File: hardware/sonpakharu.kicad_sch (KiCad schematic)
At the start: 66 parts, among them IC1 ESP32-S3-WROOM-1U-N4, J1 ADC4, J10 EXT2, J11 EXT3, J12 BATT, J13 EXT7, J14 PWR, J15 EXT8, J16 485, J17 FTDI, J2 ADC3, J3 ADC2, J4 ADC1, J5 EXT4, J6 I2C, J7 EXT5, J8 EXT1, J9 EXT6, Q1 DMG3415U, Q2 S8050, Q3 S8050, Q4 S8050, SW1 Boot, SW2 Reset, U1 AP2112K-3.3TRG1, U2 MCP73831-2-OT, U3 MAX485E, U4 ADS1115IDGSR

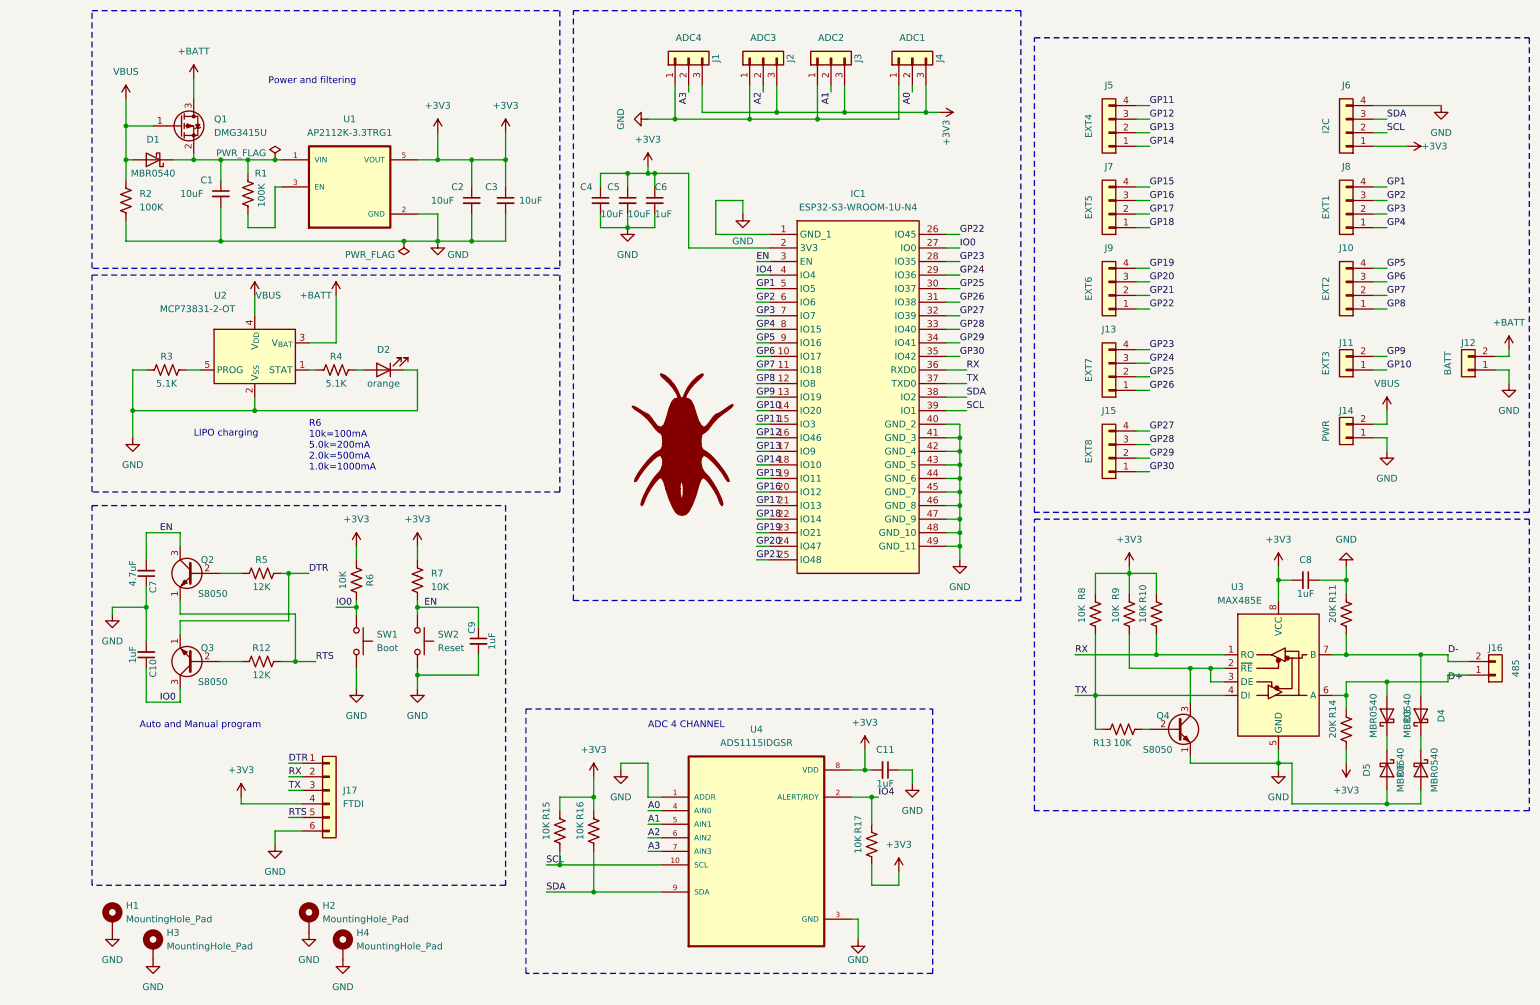
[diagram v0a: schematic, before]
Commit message: Fix: foot prints, re routed pcb, added 3d model
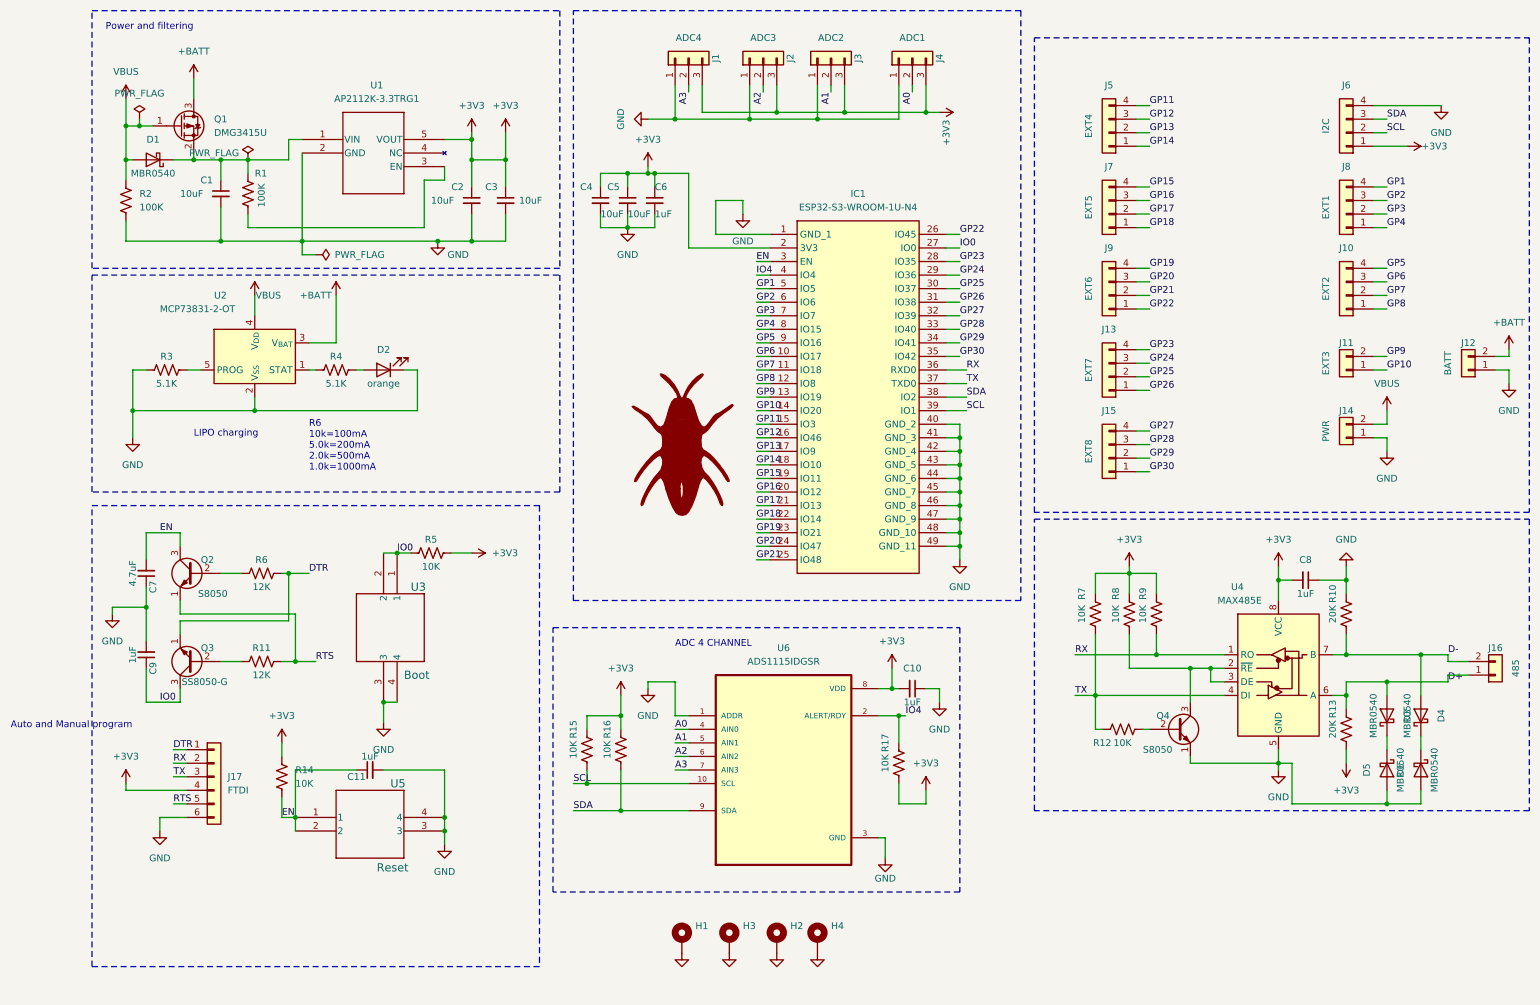
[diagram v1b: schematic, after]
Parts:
- removed SW1: Boot, Button_Switch_SMD:SW_Push_1P1T_NO_6x6mm_H9.5mm, symbol Switch:SW_Push
- removed SW2: Reset, Button_Switch_SMD:SW_Push_1P1T_NO_6x6mm_H9.5mm, symbol Switch:SW_Push
- added U3: Boot, PTS526 SK15 SMTR2 LFS:SMT_FS, symbol PTS526 SK15 SMTR2 LFS:PTS526_SK15_SMTR2_LFS
- added U5: Reset, PTS526 SK15 SMTR2 LFS:SMT_FS, symbol PTS526 SK15 SMTR2 LFS:PTS526_SK15_SMTR2_LFS
- H2: value MountingHole_Pad -> mounting hole
- Q3: value S8050 -> SS8050-G
- U1: footprint AP2112K-3.3TRG1:SOT95P285X140-5N -> AP2112K_3_3TRG1:SOT25; symbol AP2112K-3.3TRG1:AP2112K-3.3TRG1 -> AP2112K_3_3TRG1:AP2112K-3.3TRG1
- U4: renamed from U3; footprint Package_SO:SOP-8_3.9x4.9mm_P1.27mm -> Package_SO:SOIC-8_3.9x4.9mm_P1.27mm
- U6: renamed from U4; footprint ADS1115IDGSR:SOP50P490X110-10N -> Package_SO:VSSOP-10_3x3mm_P0.5mm
- renumbered C11 to C10, C9 to C11, C10 to C9, R11 to R10, R12 to R11, R13 to R12, R14 to R13, R7 to R14, R6 to R5, R5 to R6, R8 to R7, R9 to R8, R10 to R9
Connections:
- net +3V3: now also R5.2; no longer R5.1
- net EN: now also U5.1, U5.2
- net GND: now also U3.3, U3.4, U5.3, U5.4
- net IO0: now also R5.1, U3.1, U3.2; no longer R5.2
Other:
- moved on the sheet: C10, C11, H1, H2, H3, H4, J17, R14, R15, R16, R17, R5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

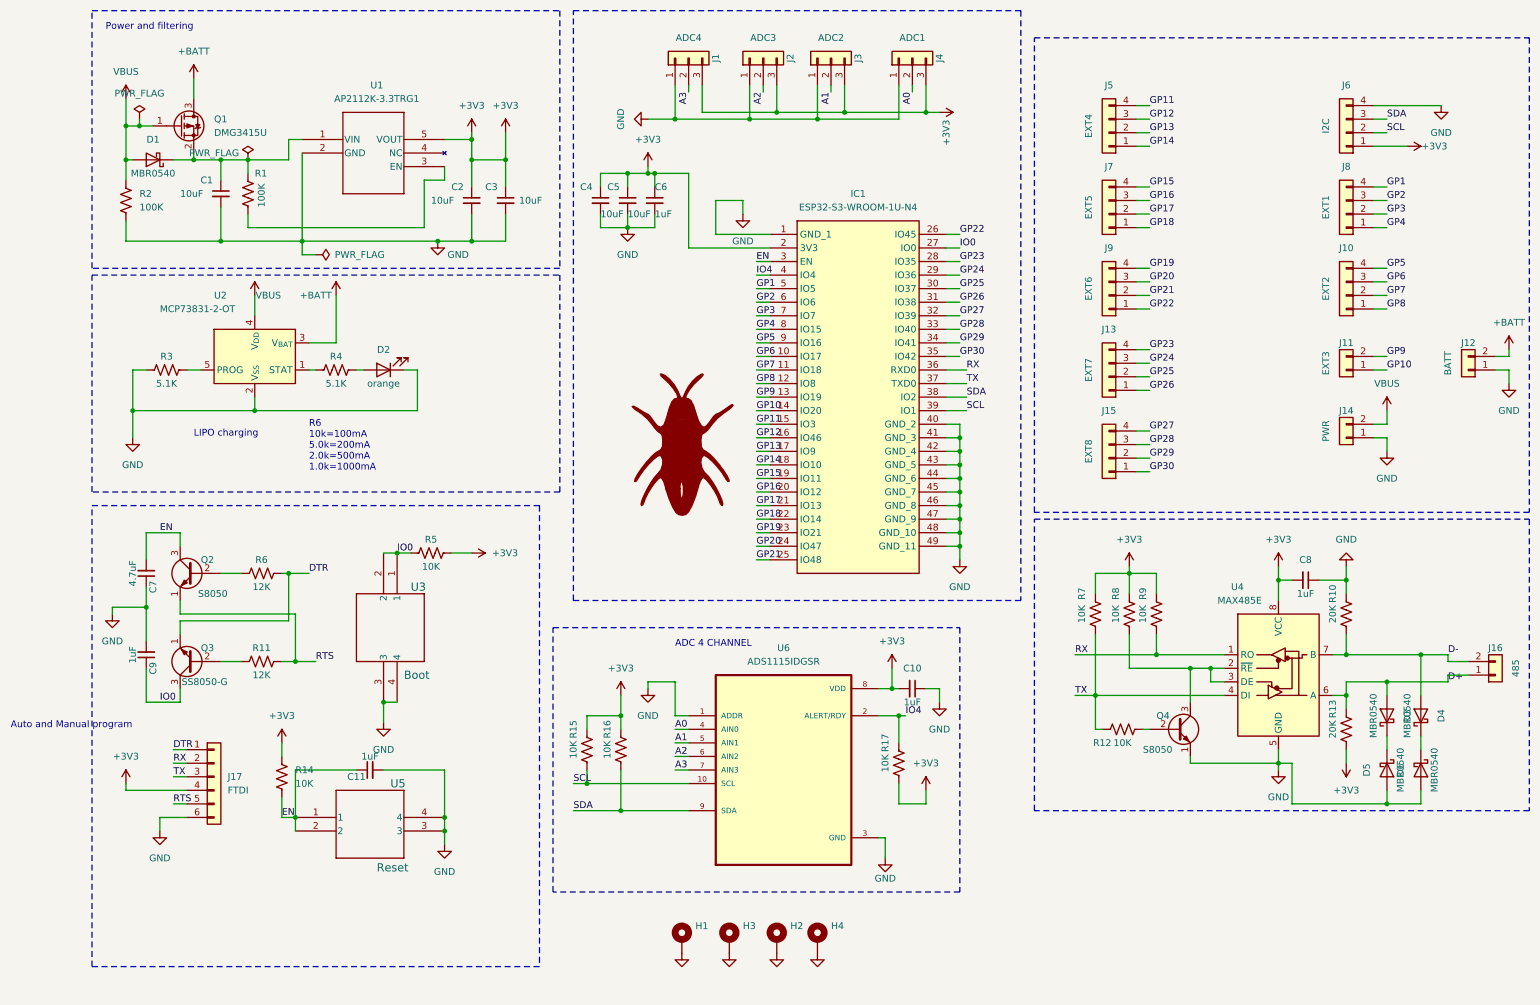
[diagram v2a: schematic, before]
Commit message: rectified sch
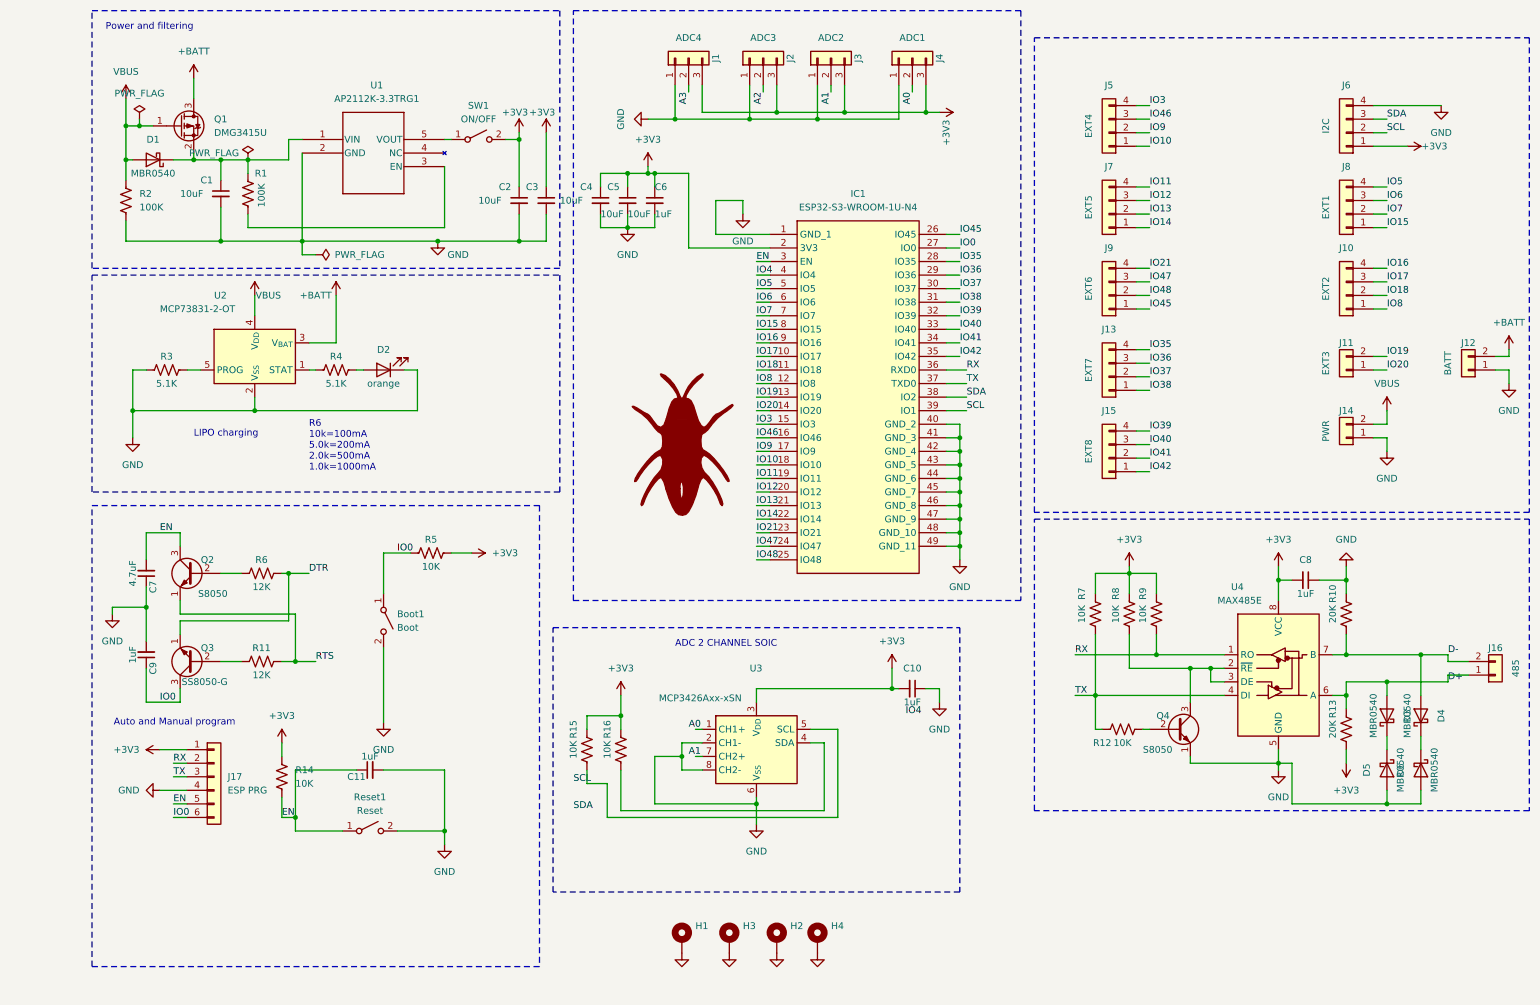
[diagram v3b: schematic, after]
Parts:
- removed R17: 10K, Resistor_SMD:R_0603_1608Metric, symbol Device:R_US
- removed U3: Boot, PTS526 SK15 SMTR2 LFS:SMT_FS, symbol PTS526 SK15 SMTR2 LFS:PTS526_SK15_SMTR2_LFS
- removed U5: Reset, PTS526 SK15 SMTR2 LFS:SMT_FS, symbol PTS526 SK15 SMTR2 LFS:PTS526_SK15_SMTR2_LFS
- removed U6: ADS1115IDGSR, Package_SO:VSSOP-10_3x3mm_P0.5mm, symbol ADS1115IDGSR:ADS1115IDGSR
- added Boot1: Boot, tactile_5.4:tactile_5.4, symbol Switch:SW_SPST
- added Reset1: Reset, tactile_5.4:tactile_5.4, symbol Switch:SW_SPST
- added SW1: ON/OFF, Connector_PinHeader_2.54mm:PinHeader_1x02_P2.54mm_Vertical, symbol Switch:SW_SPST
- added U3: MCP3426Axx-xSN, Package_SO:SOIC-8_3.9x4.9mm_P1.27mm, symbol Analog_ADC:MCP3426Axx-xSN
- C1, C10, C11, C2, C3, C4, C6, C7, C8, C9: footprint Capacitor_SMD:C_0603_1608Metric -> Capacitor_SMD:C_0805_2012Metric
- D2: footprint LED_SMD:LED_0603_1608Metric -> LED_SMD:LED_1206_3216Metric
- J17: value FTDI -> ESP PRG
- R1, R10, R11, R12, R13, R14, R15, R2, R3, R4, R5, R6, R7, R8, R9: footprint Resistor_SMD:R_0603_1608Metric -> Resistor_SMD:R_0805_2012Metric
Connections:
- net +3V3: now also J17.1 (Pin_1), SW1.2 (B), U3.3 (V_{DD}); no longer J17.4 (Pin_4), U1.5 (VOUT)
- net DTR: no longer J17.1 (Pin_1)
- net EN: now also J17.5 (Pin_5), Reset1.1 (A)
- net GND: now also J17.4 (Pin_4), Boot1.2 (B), Reset1.2 (B), U3.2 (CH1-), U3.6 (V_{SS}), U3.8 (CH2-); no longer J17.6 (Pin_6)
- net IO0: now also J17.6 (Pin_6), Boot1.1 (A)
- net RTS: no longer J17.5 (Pin_5)
- net SCL: no longer R15.2
- net SDA: no longer R16.2
- net GP1 renamed IO5
- net GP10 renamed IO20
- net GP11 renamed IO3
- net GP12 renamed IO46
- net GP13 renamed IO9
- net GP14 renamed IO10
- net GP15 renamed IO11
- net GP16 renamed IO12
- net GP17 renamed IO13
- net GP18 renamed IO14
- net GP19 renamed IO21
- net GP2 renamed IO6
- net GP20 renamed IO47
- net GP21 renamed IO48
- net GP22 renamed IO45
- net GP23 renamed IO35
- net GP24 renamed IO36
- net GP25 renamed IO37
- net GP26 renamed IO38
- net GP27 renamed IO39
- net GP28 renamed IO40
- net GP29 renamed IO41
- net GP3 renamed IO7
- net GP30 renamed IO42
- net GP4 renamed IO15
- net GP5 renamed IO16
- net GP6 renamed IO17
- net GP7 renamed IO18
- net GP8 renamed IO8
- net GP9 renamed IO19
- new net: R15.2, U3.5 (SCL)
- new net: SW1.1 (A), U1.5 (VOUT)
- new net: R16.2, U3.4 (SDA)
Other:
- note added: "ADC 2 CHANNEL SOIC"
- note removed: "ADC 4 CHANNEL"
- moved on the sheet: C2, C3

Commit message: removed auto prg ckt, done routing, touch up pending
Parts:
- removed C7: 4.7uF, Capacitor_SMD:C_0805_2012Metric, symbol Device:C_Small
- removed C9: 1uF, Capacitor_SMD:C_0805_2012Metric, symbol Device:C_Small
- removed J1: ADC4, Connector_Molex:Molex_KK-254_AE-6410-03A_1x03_P2.54mm_Vertical, symbol Connector_Generic:Conn_01x03
- removed J2: ADC3, Connector_Molex:Molex_KK-254_AE-6410-03A_1x03_P2.54mm_Vertical, symbol Connector_Generic:Conn_01x03
- removed Q2: S8050, Package_TO_SOT_SMD:SOT-23, symbol Transistor_BJT:S8050
- removed Q3: SS8050-G, Package_TO_SOT_SMD:SOT-23, symbol Transistor_BJT:S8050
- removed R11, R6: 12K, Resistor_SMD:R_0805_2012Metric, symbol Device:R_US
- C5: footprint Capacitor_SMD:C_0603_1608Metric -> Capacitor_SMD:C_0805_2012Metric
- R16: footprint Resistor_SMD:R_0603_1608Metric -> Resistor_SMD:R_0805_2012Metric
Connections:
- net A0: now also U3.1 (CH1+)
- net A1: now also U3.7 (CH2+)

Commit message: rectified sda scl lines
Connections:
- net SCL: now also R15.2, U3.5 (SCL)
- net SDA: now also R16.2, U3.4 (SDA)
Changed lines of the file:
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@@
 	)
 	(junction
+		(at 149.86 152.4)
+		(diameter 0)
+		(color 0 0 0 0)
+	)
+	(junction
 		(at 255.27 163.83)
 		(diameter 0)
@@
 	)
 	(junction
+		(at 152.4 149.86)
+		(diameter 0)
+		(color 0 0 0 0)
+	)
+	(junction
 		(at 222.25 138.43)
 		(diameter 0)
@@
 	(wire
 		(pts
+			(xy 152.4 149.86) (xy 154.94 149.86)
+		)
+		(stroke
+			(width 0)
+			(type default)
+		)
+	)
+	(wire
+		(pts
 			(xy 255.27 151.13) (xy 255.27 153.67)
 		)
@@
 	(wire
 		(pts
+			(xy 149.86 152.4) (xy 154.94 152.4)
+		)
+		(stroke
+			(width 0)
+			(type default)
+		)
+	)
+	(wire
+		(pts
 			(xy 31.75 41.91) (xy 31.75 43.18)
 		)
@@
 		)
 	)
-	(label "SDA"
-		(at 102.87 165.1 0)
-		(fields_autoplaced yes)
-		(effects
-			(font
-				(size 1.27 1.27)
-			)
-			(justify left bottom)
-		)
-	)
 	(label "IO0"
 		(at 175.26 59.69 0)
@@
 		)
 	)
-	(label "SCL"
-		(at 102.87 160.02 0)
-		(fields_autoplaced yes)
-		(effects
-			(font
-				(size 1.27 1.27)
-			)
-			(justify left bottom)
-		)
-	)
 	(label "IO5"
 		(at 255.27 48.26 0)
@@
 		)
 	)
+	(label "SDA"
+		(at 154.94 152.4 0)
+		(fields_autoplaced yes)
+		(effects
+			(font
+				(size 1.27 1.27)
+			)
+			(justify left bottom)
+		)
+	)
 	(label "IO10"
 		(at 210.82 40.64 0)
@@
 		(fields_autoplaced yes)
 		(effects
+			(font
+				(size 1.27 1.27)
+			)
+			(justify left bottom)
+		)
+	)
+	(label "SCL"
+		(at 154.94 149.86 0)
+		(fields_autoplaced yes)
+		(effects
